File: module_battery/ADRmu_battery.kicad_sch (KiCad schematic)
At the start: 30 parts, among them J1 Harting 09042326831, Q101 Q_NMOS_GDS, Q102 Q_NMOS_GDS, U101 BQ77915

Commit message: asdf
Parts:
- added C111: 100n 50V, Capacitor_SMD:C_0805_2012Metric, symbol Device:C
- added D101: 1N4148, Diode_SMD:D_SOD-123, symbol Device:D
- added D102: 16V, Diode_SMD:D_SOT-23_ANK, symbol Device:D_Zener
- added R115: 1M, Resistor_SMD:R_0805_2012Metric, symbol Device:R
- added R?: 200k, Resistor_SMD:R_0805_2012Metric, symbol Device:R
- added R? (x3): 10k, Resistor_SMD:R_0805_2012Metric, symbol Device:R
- added TH?: Thermistor_NTC, Resistor_SMD:R_0805_2012Metric, symbol Device:Thermistor_NTC
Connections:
- net GND: now also U101.23 (CTRC), U101.24 (CTRD), R?.1, R?.1, TH?.2
- net at Q102.3 (S), R113.1, R114.1: now also C111.2, D102.2 (A)
- net at Q101.3 (S), R108.2, R109.1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: now also C111.1
- net AVDD: now reaches C107.2, U101.2 (AVDD)
- net AVDD: now also U101.20 (CCFG)
- net at C106.1, R101.2, U101.1 (VDD): now also R?.2
- net at Q102.1 (G), R113.2: now also D101.1 (K), D102.1 (K), R115.2; no longer R112.1
- net at R112.2: now also D101.2 (A), R115.1; no longer U101.13 (CHG)
- net at U101.16 (CBI): now also R?.2
- net at U101.17 (OCDP): now also R?.2
- net at U101.18 (TS): now also R?.1, TH?.1
- net at U101.19 (VTB): now also R?.2
- net at U101.22 (PRES): now also R?.1
- new net: R112.1, U101.13 (CHG)
- no-connect marks 0 -> 2
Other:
- moved on the sheet: R112, R114

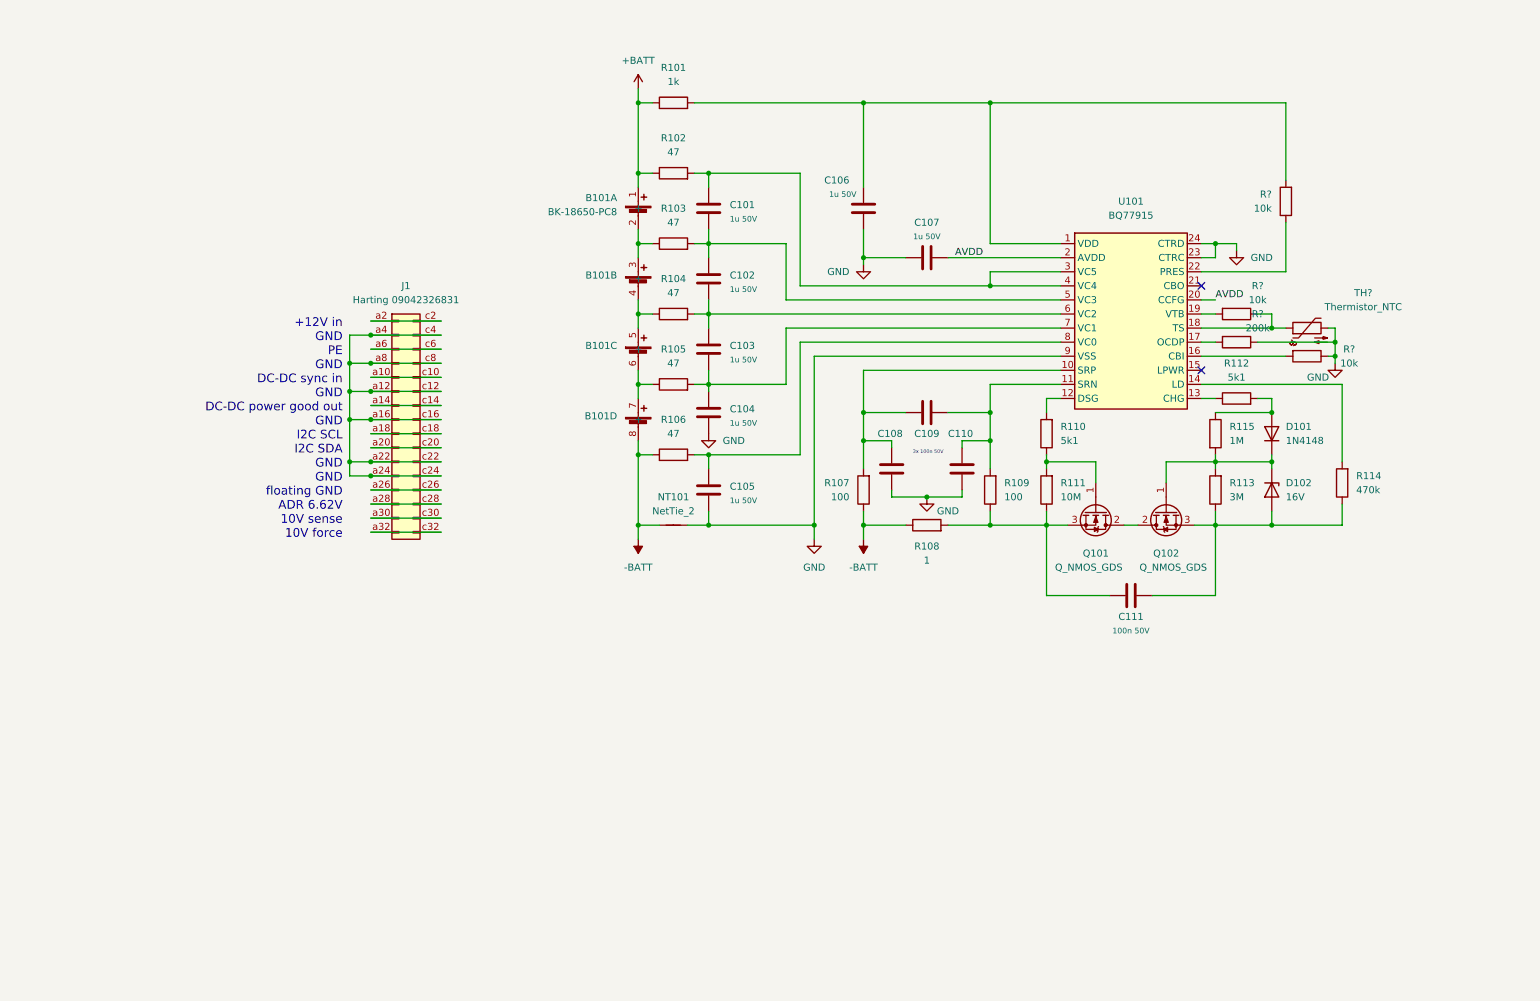
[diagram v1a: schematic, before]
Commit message: backplane connector changes
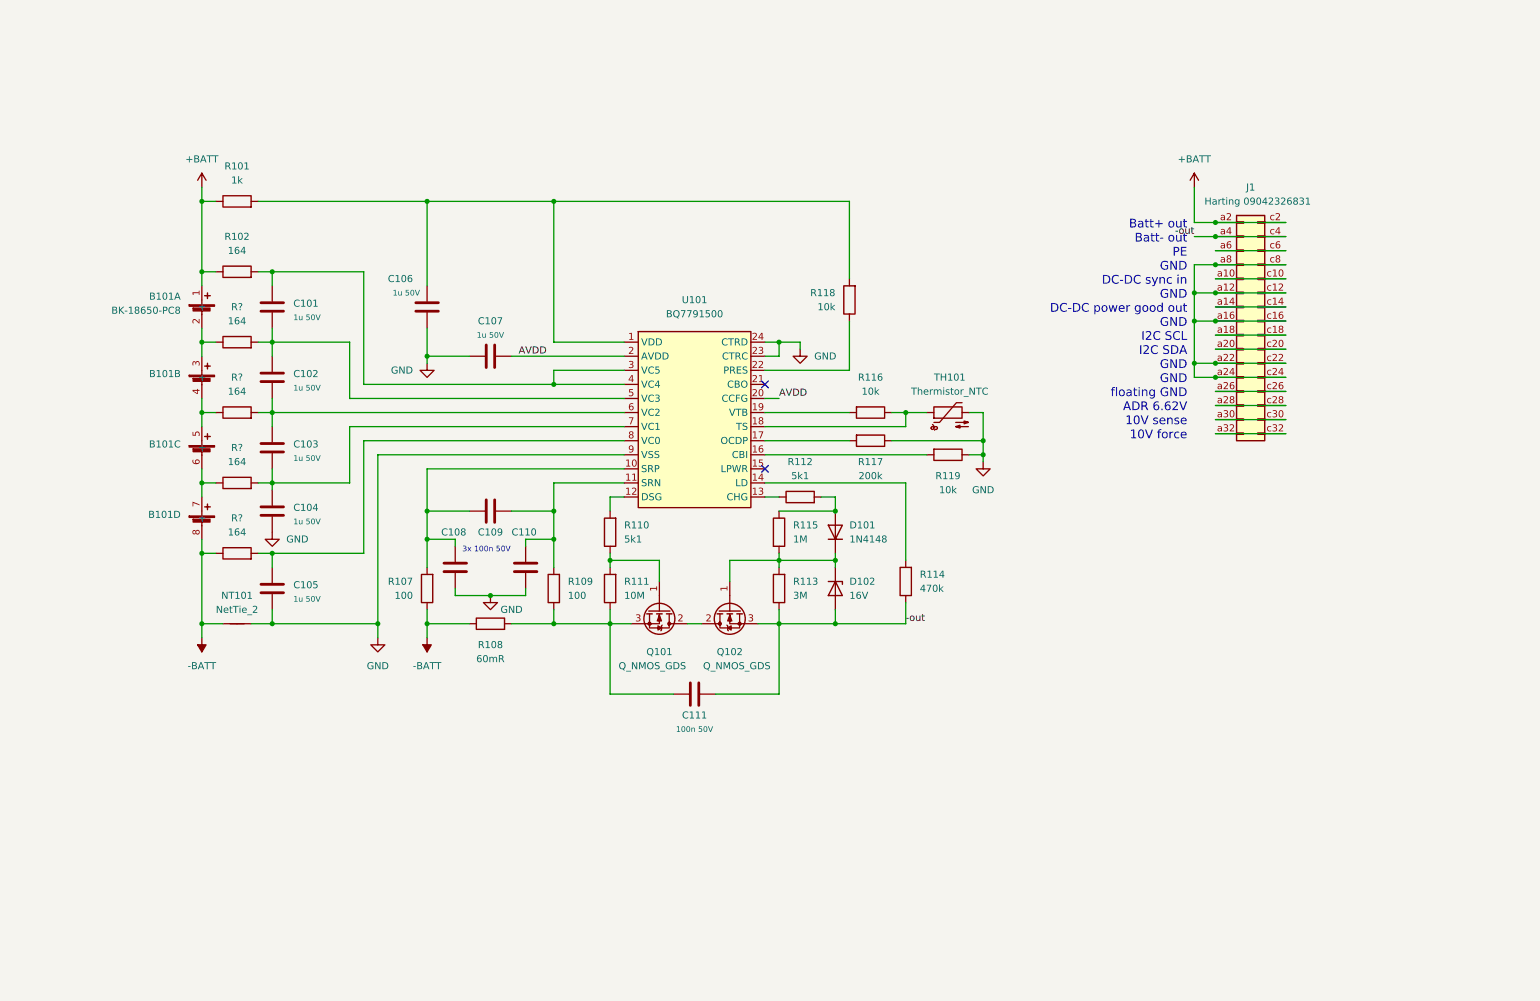
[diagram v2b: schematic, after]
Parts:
- removed R103, R104, R105, R106: 47, Resistor_SMD:R_0805_2012Metric, symbol Device:R
- added R? (x4): 164, Resistor_SMD:R_0805_2012Metric, symbol Device:R
- R102: value 47 -> 164
- R108: value 1 -> 60mR
- U101: value BQ77915 -> BQ7791500
- gave numbers to parts that had none: 5
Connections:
- net +BATT: now also J1.a2 (Pin_a2), J1.c2 (Pin_c2)
- net -BATT: now also R?.1
- net -out: now reaches C111.2, D102.2 (A), Q102.3 (S), R113.1, R114.1
- net -out: now also J1.a4 (Pin_a4), J1.c4 (Pin_c4)
- net at C105.1, U101.8 (VC0): now also R?.2
- net at C102.2, C103.1, U101.6 (VC2): now also R?.2
- net at C103.2, C104.1, U101.7 (VC1): now also R?.2
- net at J1.a12 (Pin_a12), J1.a16 (Pin_a16), J1.a22 (Pin_a22)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: no longer J1.a4 (Pin_a4), J1.c4 (Pin_c4)
- net at B101.6 (-), B101.7 (+): now also R?.1
- net at B101.4 (-), B101.5 (+): now also R?.1
- net at C101.2, C102.1, U101.5 (VC3): now also R?.2
- net at B101.2 (-), B101.3 (+): now also R?.1
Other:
- note added: "Batt+ out Batt- out PE GND DC-DC sync in GND DC-DC power good out GND I2C SCL I2C SDA GND GND floating GND ADR 6.62V 10V sense 10V force"
- note removed: "+12V in GND PE GND DC-DC sync in GND DC-DC power good out GND I2C SCL I2C SDA GND GND floating GND ADR 6.62V 10V sense 10V force"
- moved on the sheet: B101A, B101B, B101C, B101D, C101, C102, C103, C104, C105, C106, C107, C108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

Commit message: asdf
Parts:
- added C112: 100n 50V, Capacitor_SMD:C_0805_2012Metric, symbol Device:C
- added D103, D104: LT Y8SG-V2AB-36, LED_SMD:LED_1206_3216Metric, symbol Device:LED
- added R120, R122: 10k, Resistor_SMD:R_0805_2012Metric, symbol Device:R
- added R121: 1R4 2W, Resistor_SMD:R_2512_6332Metric, symbol Device:R
- added U102: LM317_TO-263, Package_TO_SOT_SMD:TO-263-2, symbol Regulator_Linear:LM317_TO-263
- gave numbers to parts that had none: 4
- renumbered C108 to C107, C107 to C108, J1 to J101, R115 to R112, R112 to R114, R118 to R115, R114 to R118
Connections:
- net +BATT: now also R120.1, R121.2, U102.1 (ADJ)
- net -out: now also D103.1 (K)
- net GND: now also J101.a22 (Pin_a22), J101.a24 (Pin_a24), J101.c22 (Pin_c22), J101.c24 (Pin_c24), C112.1, D104.1 (K)
- net at J101.a10 (Pin_a10): no longer J101.c10 (Pin_c10)
- net at J101.a14 (Pin_a14): no longer J101.c14 (Pin_c14)
- net at J101.a18 (Pin_a18): no longer J101.c18 (Pin_c18)
- net in+: now reaches J101.a20 (Pin_a20), J101.c20 (Pin_c20)
- net in+: now also C112.2, R122.1, U102.3 (VI)
- net at J101.a26 (Pin_a26): no longer J101.c26 (Pin_c26)
- net at J101.a28 (Pin_a28): no longer J101.c28 (Pin_c28)
- net at J101.a30 (Pin_a30): no longer J101.c30 (Pin_c30)
- net at J101.a32 (Pin_a32): no longer J101.c32 (Pin_c32)
- net at J101.a6 (Pin_a6): no longer J101.c6 (Pin_c6)
- new net: D103.2 (A), R120.2
- new net: R121.1, U102.2 (VO)
- new net: D104.2 (A), R122.2
- now unconnected: J101.a12 (Pin_a12), J101.a16 (Pin_a16), J101.a8 (Pin_a8), J101.c12 (Pin_c12), J101.c16 (Pin_c16), J101.c8 (Pin_c8)
- no-connect marks 2 -> 24
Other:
- note added: "Batt+ out Batt- out NC NC NC NC NC NC NC In+ In- PE NC NC NC NC"
- note removed: "Batt+ out Batt- out PE GND DC-DC sync in GND DC-DC power good out GND I2C SCL I2C SDA GND GND floating GND ADR 6.62V 10V sense 10V force"
- moved on the sheet: B101A, B101B, B101C, B101D, C101, C102, C103, C104, C105, C106, C107, C108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

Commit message: Battery charger Rev 0.1 finished
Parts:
- added H101, H102, H103, H104: MountingHole, MountingHole:MountingHole_4.3mm_M4, symbol Mechanical:MountingHole
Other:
- company: (none) -> RPG
- title: (none) -> ADRmu battery module
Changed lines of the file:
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@@
 (kicad_sch (version 20211123) (generator eeschema)
   (paper "A4")
+  (title_block
+    (title "ADRmu battery module")
+    (date "2022-02-14")
+    (rev "0.1")
+    (company "RPG")
+    (comment 1 "All resistors 0.1% MF unless otherwise noted")
+    (comment 2 "All capacitors X7R MLCC unless otherwise noted")
+  )
   (junction (at 149.86 102.87) (diameter 0) (color 0 0 0 0)
   )
@@
     (pin "1")
     (pin "2")
+  )
+  (symbol (lib_id "Mechanical:MountingHole") (at 250.19 140.97 0) (unit 1)
+    (in_bom no) (on_board yes) (fields_autoplaced)
+    (property "Reference" "H103" (id 0) (at 247.65 139.6999 0)
+      (effects (font (size 1.27 1.27)) (justify right))
+    )
+    (property "Value" "MountingHole" (id 1) (at 247.65 142.2399 0)
+      (effects (font (size 1.27 1.27)) (justify right))
+    )
+    (property "Footprint" "MountingHole:MountingHole_4.3mm_M4" (id 2) (at 250.19 140.97 0)
+      (effects (font (size 1.27 1.27)) hide)
+    )
+    (property "Datasheet" "~" (id 3) (at 250.19 140.97 0)
+      (effects (font (size 1.27 1.27)) hide)
+    )
   )
   (symbol (lib_id "Device:C") (at 48.26 82.55 0) (unit 1)
@@
     (pin "2")
   )
+  (symbol (lib_id "Mechanical:MountingHole") (at 252.73 128.27 0) (unit 1)
+    (in_bom no) (on_board yes) (fields_autoplaced)
+    (property "Reference" "H104" (id 0) (at 250.19 126.9999 0)
+      (effects (font (size 1.27 1.27)) (justify right))
+    )
+    (property "Value" "MountingHole" (id 1) (at 250.19 129.5399 0)
+      (effects (font (size 1.27 1.27)) (justify right))
+    )
+    (property "Footprint" "MountingHole:MountingHole_4.3mm_M4" (id 2) (at 252.73 128.27 0)
+      (effects (font (size 1.27 1.27)) hide)
+    )
+    (property "Datasheet" "~" (id 3) (at 252.73 128.27 0)
+      (effects (font (size 1.27 1.27)) hide)
+    )
+  )
   (symbol (lib_id "ADRmu_battery_Library:BK-18650-PC8") (at 35.56 95.25 0) (unit 4)
     (in_bom yes) (on_board yes) (fields_autoplaced)
@@
     (pin "1")
     (pin "2")
+  )
+  (symbol (lib_id "Mechanical:MountingHole") (at 234.95 128.27 0) (unit 1)
+    (in_bom no) (on_board yes) (fields_autoplaced)
+    (property "Reference" "H102" (id 0) (at 232.41 126.9999 0)
+      (effects (font (size 1.27 1.27)) (justify right))
+    )
+    (property "Value" "MountingHole" (id 1) (at 232.41 129.5399 0)
+      (effects (font (size 1.27 1.27)) (justify right))
+    )
+    (property "Footprint" "MountingHole:MountingHole_4.3mm_M4" (id 2) (at 234.95 128.27 0)
+      (effects (font (size 1.27 1.27)) hide)
+    )
+    (property "Datasheet" "~" (id 3) (at 234.95 128.27 0)
+      (effects (font (size 1.27 1.27)) hide)
+    )
   )
   (symbol (lib_id "power:GND") (at 248.92 83.82 0) (unit 1)
@@
     (pin "2")
   )
+  (symbol (lib_id "Mechanical:MountingHole") (at 232.41 140.97 0) (unit 1)
+    (in_bom no) (on_board yes) (fields_autoplaced)
+    (property "Reference" "H101" (id 0) (at 229.87 139.6999 0)
+      (effects (font (size 1.27 1.27)) (justify right))
+    )
+    (property "Value" "MountingHole" (id 1) (at 229.87 142.2399 0)
+      (effects (font (size 1.27 1.27)) (justify right))
+    )
+    (property "Footprint" "MountingHole:MountingHole_4.3mm_M4" (id 2) (at 232.41 140.97 0)
+      (effects (font (size 1.27 1.27)) hide)
+    )
+    (property "Datasheet" "~" (id 3) (at 232.41 140.97 0)
+      (effects (font (size 1.27 1.27)) hide)
+    )
+  )
   (symbol (lib_id "power:+BATT") (at 35.56 34.29 0) (unit 1)
     (in_bom yes) (on_board yes) (fields_autoplaced)
@@
       (reference "D104") (unit 1) (value "LT Y8SG-V2AB-36") (footprint "LED_SMD:LED_1206_3216Metric")
     )
+    (path "/e94817df-7d70-47d0-862c-8c59dfc32761"
+      (reference "H101") (unit 1) (value "MountingHole") (footprint "MountingHole:MountingHole_4.3mm_M4")
+    )
+    (path "/8233de19-691a-4981-9177-f647c5ab854c"
+      (reference "H102") (unit 1) (value "MountingHole") (footprint "MountingHole:MountingHole_4.3mm_M4")
+    )
+    (path "/3532dee9-6e3a-45a8-875d-a70e3d243b65"
+      (reference "H103") (unit 1) (value "MountingHole") (footprint "MountingHole:MountingHole_4.3mm_M4")
+    )
+    (path "/624700dd-baae-4a20-a2e6-b73e4b0e622b"
+      (reference "H104") (unit 1) (value "MountingHole") (footprint "MountingHole:MountingHole_4.3mm_M4")
+    )
     (path "/59fbe416-3cd9-436b-a19d-e1b1ddce22ac"

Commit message: dimmed LED brightness and started to fix a few first generation battery bug fixes
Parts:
- added D?: 1N4001, Diode_THT:D_DO-41_SOD81_P10.16mm_Horizontal, symbol Diode:1N4001
- R120, R122: value 10k -> 16k9
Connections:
- net +BATT: now also D?.1 (K); no longer R121.2
- net GND: no longer J101.a22 (Pin_a22), J101.c22 (Pin_c22)
- net -out renamed -i/o
- net -i/o: now also J101.a22 (Pin_a22), J101.c22 (Pin_c22)
- new net: D?.2 (A), R121.2
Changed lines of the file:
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@@
   (junction (at 139.7 114.3) (diameter 0) (color 0 0 0 0)
   )
+  (junction (at 177.8 38.1) (diameter 0) (color 0 0 0 0)
+  )
   (junction (at 48.26 114.3) (diameter 0) (color 0 0 0 0)
   )
@@
   (junction (at 48.26 101.6) (diameter 0) (color 0 0 0 0)
   )
-  (junction (at 185.42 38.1) (diameter 0) (color 0 0 0 0)
-  )
   (junction (at 149.86 114.3) (diameter 0) (color 0 0 0 0)
   )
@@
   )
   (junction (at 176.53 81.28) (diameter 0) (color 0 0 0 0)
-  )
-  (junction (at 248.92 82.55) (diameter 0) (color 0 0 0 0)
   )
   (junction (at 139.7 102.87) (diameter 0) (color 0 0 0 0)
@@
   (no_connect (at 137.16 86.36))
   (no_connect (at 137.16 71.12))
-  (wire (pts (xy 248.92 80.01) (xy 248.92 82.55))
-    (stroke (width 0) (type default) (color 0 0 0 0))
-  )
   (wire (pts (xy 248.92 77.47) (xy 254 77.47))
     (stroke (width 0) (type default) (color 0 0 0 0))
@@
     (stroke (width 0) (type default) (color 0 0 0 0))
   )
+  (wire (pts (xy 186.69 38.1) (xy 187.96 38.1))
+    (stroke (width 0) (type default) (color 0 0 0 0))
+  )
   (wire (pts (xy 64.77 81.28) (xy 111.76 81.28))
     (stroke (width 0) (type default) (color 0 0 0 0))
@@
     (stroke (width 0) (type default) (color 0 0 0 0))
   )
-  (wire (pts (xy 185.42 38.1) (xy 185.42 48.26))
-    (stroke (width 0) (type default) (color 0 0 0 0))
-  )
   (wire (pts (xy 149.86 91.44) (xy 149.86 93.98))
     (stroke (width 0) (type default) (color 0 0 0 0))
@@
     (stroke (width 0) (type default) (color 0 0 0 0))
   )
+  (wire (pts (xy 177.8 38.1) (xy 179.07 38.1))
+    (stroke (width 0) (type default) (color 0 0 0 0))
+  )
   (wire (pts (xy 99.06 114.3) (xy 109.22 114.3))
     (stroke (width 0) (type default) (color 0 0 0 0))
@@
     (stroke (width 0) (type default) (color 0 0 0 0))
   )
-  (wire (pts (xy 185.42 35.56) (xy 185.42 38.1))
+  (wire (pts (xy 177.8 35.56) (xy 177.8 38.1))
     (stroke (width 0) (type default) (color 0 0 0 0))
   )
@@
     (stroke (width 0) (type default) (color 0 0 0 0))
   )
-  (wire (pts (xy 187.96 38.1) (xy 185.42 38.1))
-    (stroke (width 0) (type default) (color 0 0 0 0))
-  )
   (wire (pts (xy 76.2 66.04) (xy 83.82 66.04))
     (stroke (width 0) (type default) (color 0 0 0 0))
@@
     (stroke (width 0) (type default) (color 0 0 0 0))
   )
-  (wire (pts (xy 185.42 48.26) (xy 205.74 48.26))
+  (wire (pts (xy 177.8 48.26) (xy 205.74 48.26))
+    (stroke (width 0) (type default) (color 0 0 0 0))
+  )
+  (wire (pts (xy 177.8 38.1) (xy 177.8 48.26))
     (stroke (width 0) (type default) (color 0 0 0 0))
   )
@@
     (effects (font (size 1.27 1.27)) (justify right bottom))
   )
-  (label "-out" (at 248.92 57.15 180)
+  (label "-i{slash}o" (at 248.92 57.15 180)
     (effects (font (size 1.27 1.27)) (justify right bottom))
   )
-  (label "-out" (at 162.56 114.3 0)
+  (label "-i{slash}o" (at 248.92 80.01 180)
+    (effects (font (size 1.27 1.27)) (justify right bottom))
+  )
+  (label "-i{slash}o" (at 162.56 114.3 0)
     (effects (font (size 1.27 1.27)) (justify left bottom))
   )
@@
     (pin "2")
   )
-  (symbol (lib_id "power:+BATT") (at 185.42 35.56 0) (unit 1)
-    (in_bom yes) (on_board yes) (fields_autoplaced)
-    (property "Reference" "#PWR0111" (id 0) (at 185.42 39.37 0)
-      (effects (font (size 1.27 1.27)) hide)
-    )
-    (property "Value" "+BATT" (id 1) (at 185.42 30.48 0))
-    (property "Footprint" "" (id 2) (at 185.42 35.56 0)
-      (effects (font (size 1.27 1.27)) hide)
-    )
-    (property "Datasheet" "" (id 3) (at 185.42 35.56 0)
+  (symbol (lib_id "power:+BATT") (at 177.8 35.56 0) (unit 1)
+    (in_bom yes) (on_board yes) (fields_autoplaced)
+    (property "Reference" "#PWR0111" (id 0) (at 177.8 39.37 0)
+      (effects (font (size 1.27 1.27)) hide)
+    )
+    (property "Value" "+BATT" (id 1) (at 177.8 30.48 0))
+    (property "Footprint" "" (id 2) (at 177.8 35.56 0)
+      (effects (font (size 1.27 1.27)) hide)
+    )
+    (property "Datasheet" "" (id 3) (at 177.8 35.56 0)
       (effects (font (size 1.27 1.27)) hide)
     )
@@
       (effects (font (size 1.27 1.27)) (justify left))
     )
-    (property "Value" "10k" (id 1) (at 179.07 101.5999 0)
+    (property "Value" "16k9" (id 1) (at 179.07 101.5999 0)
       (effects (font (size 1.27 1.27)) (justify left))
     )
@@
       (effects (font (size 1.27 1.27)) (justify left))
     )
-    (property "Value" "10k" (id 1) (at 218.44 45.7199 0)
+    (property "Value" "16k9" (id 1) (at 218.44 45.7199 0)
       (effects (font (size 1.27 1.27)) (justify left))
     )
@@
     )
     (pin "1")
+  )
+  (symbol (lib_id "Diode:1N4001") (at 182.88 38.1 0) (unit 1)
+    (in_bom yes) (on_board yes) (fields_autoplaced)
+    (property "Reference" "D?" (id 0) (at 182.88 31.75 0))
+    (property "Value" "1N4001" (id 1) (at 182.88 34.29 0))
+    (property "Footprint" "Diode_THT:D_DO-41_SOD81_P10.16mm_Horizontal" (id 2) (at 182.88 42.545 0)
+      (effects (font (size 1.27 1.27)) hide)
+    )
+    (property "Datasheet" "http://www.vishay.com/docs/88503/1n4001.pdf" (id 3) (at 182.88 38.1 0)
+      (effects (font (size 1.27 1.27)) hide)
+    )
+    (pin "1")
+    (pin "2")
   )
   (symbol (lib_id "Regulator_Linear:LM317_TO-263") (at 205.74 38.1 0) (mirror y) (unit 1)
@@
       (reference "D104") (unit 1) (value "LT Y8SG-V2AB-36") (footprint "LED_SMD:LED_1206_3216Metric")
     )
+    (path "/c564451e-5503-4bb8-ba3d-197a29ea63c6"
+      (reference "D?") (unit 1) (value "1N4001") (footprint "Diode_THT:D_DO-41_SOD81_P10.16mm_Horizontal")
+    )
     (path "/e94817df-7d70-47d0-862c-8c59dfc32761"
       (reference "H101") (unit 1) (value "MountingHole") (footprint "MountingHole:MountingHole_4.3mm_M4")
@@
     )
     (path "/6c6dd531-fab5-476d-8cae-9514a0af0247"
-      (reference "R120") (unit 1) (value "10k") (footprint "Resistor_SMD:R_0805_2012Metric")
+      (reference "R120") (unit 1) (value "16k9") (footprint "Resistor_SMD:R_0805_2012Metric")
     )
     (path "/5f62081c-0222-496a-b71e-5f8446c03bad"
@@
     )
     (path "/96b1582e-1bf5-40ee-8df6-bed2694ce633"
-      (reference "R122") (unit 1) (value "10k") (footprint "Resistor_SMD:R_0805_2012Metric")
+      (reference "R122") (unit 1) (value "16k9") (footprint "Resistor_SMD:R_0805_2012Metric")
     )
     (path "/eb79ab6e-5927-4ac1-8ae0-e3ccc79e76cf"
